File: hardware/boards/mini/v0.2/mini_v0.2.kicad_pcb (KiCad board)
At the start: 8 copper layers, 20 x 41 mm, 100 parts, among them IC1 NAU88C22YG, IC3 IS42S16160J-6BLI, J2 Top, J3 Bottom, Q1 PMV37EN22, U1 W25Q128JVP, U2 LTV-217-G, U4 STM32H750XBHx, Y1 Crystal_GND24, Y3 32.768kHz

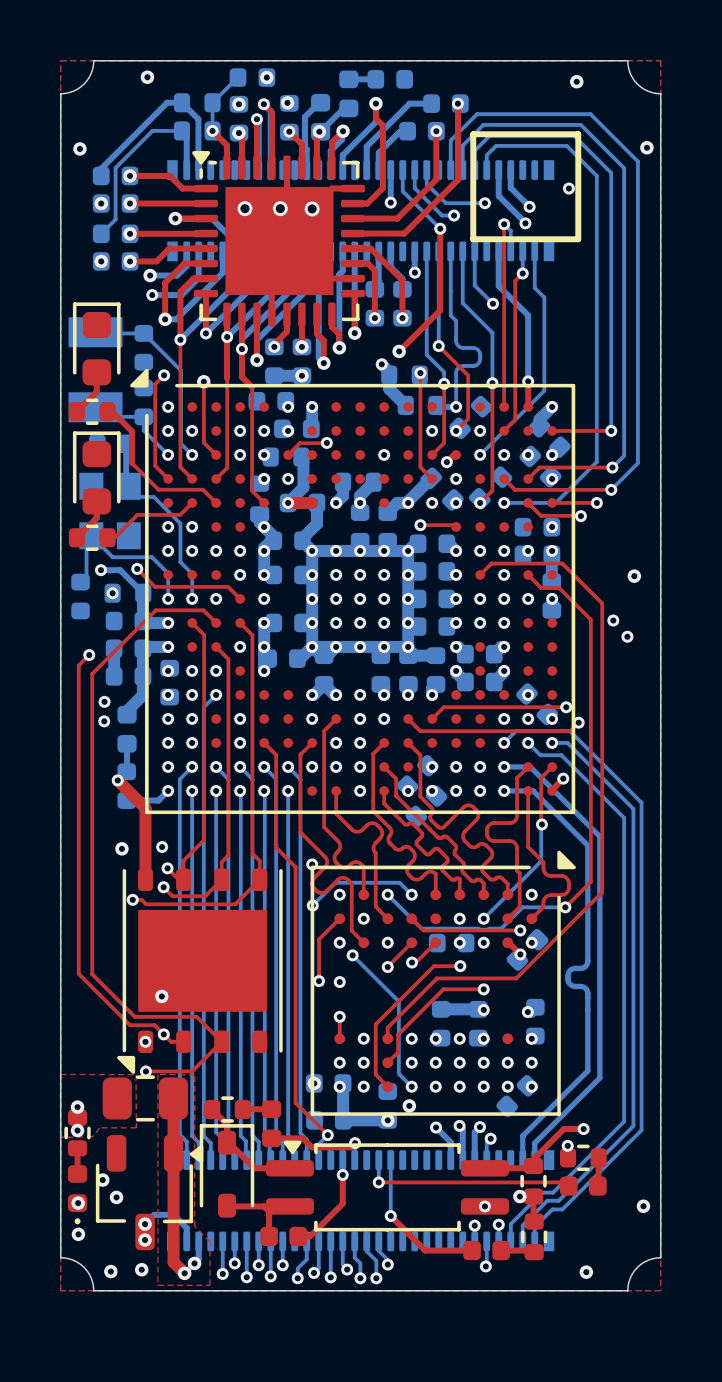
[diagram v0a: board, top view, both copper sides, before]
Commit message: mini: start adding symbol for mating footprint
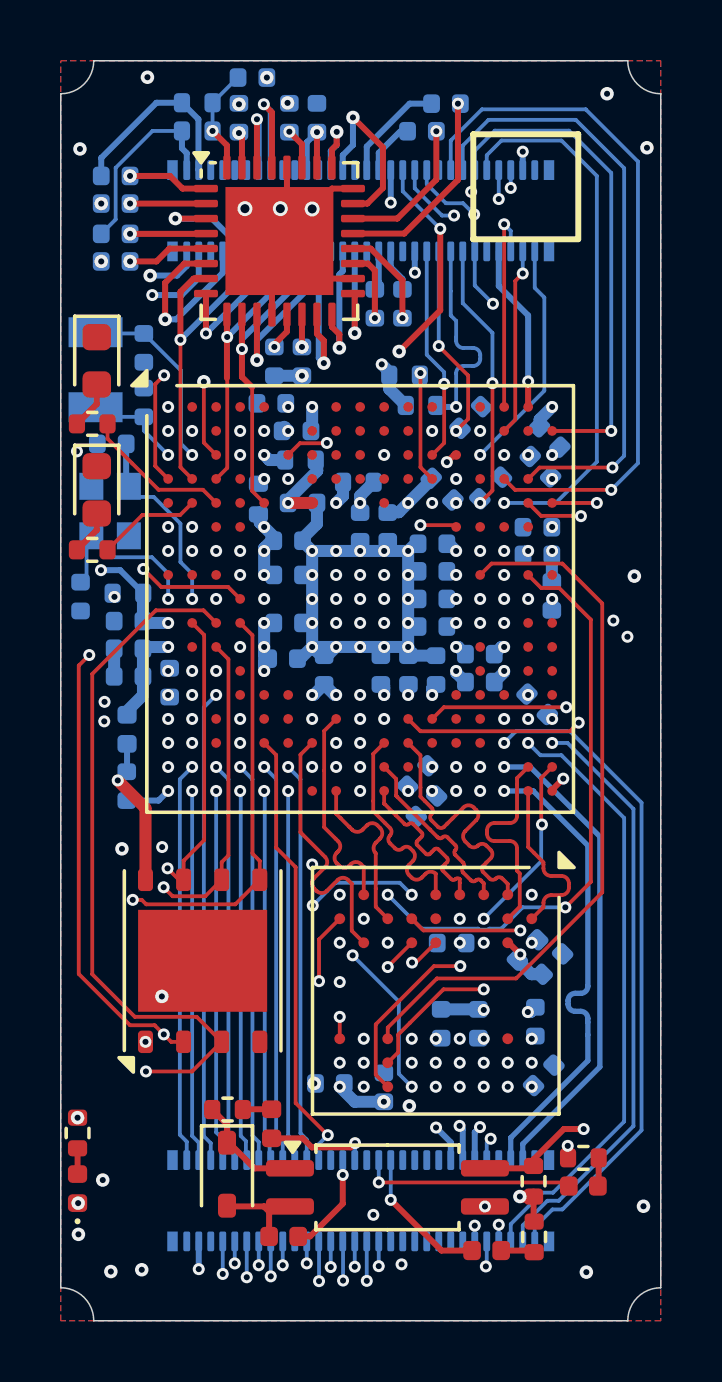
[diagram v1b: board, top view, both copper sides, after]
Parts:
- removed D5, D6: D, Diode_SMD:D_0402_1005Metric
- removed F1: Polyfuse, Fuse:Fuse_0805_2012Metric
- removed Q1: PMV37EN22, Package_TO_SOT_SMD:TSOT-23
- moved C34 9.09 mm to (86.4, 87.1), turned to 45 degrees
- moved C18 2.76 mm to (78.5, 58.9), turned to 90 degrees
- moved C13 1.12 mm to (86.1, 90.8), turned to 45 degrees
- moved C35 0.63 mm to (80.8, 91.2)
- moved R2 0.49 mm to (78.0, 70.3)
- moved D2 0.40 mm to (71.2, 67.0)
- moved R15 0.40 mm to (71.0, 69.1)
- moved D4 0.40 mm to (71.2, 71.3)
- moved R17 0.40 mm to (71.0, 73.3)
- moved C3 0.07 mm to (77.9, 69.3)
- moved C37 0.07 mm to (77.0, 68.4)
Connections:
- C18 pad 1: +3.3V -> /VDDSPK
- IC1 pad 26: Net-(D5-K) -> /VDDSPK
- J2 pad 1: unconnected-(J2-Pad1) -> GND
- J2 pad 10: unconnected-(J2-Pad10) -> GND
- J2 pad 17: unconnected-(J2-Pad17) -> GND
- J2 pad 24: unconnected-(J2-Pad24) -> GND
- J2 pad 3: unconnected-(J2-Pad3) -> +3.3V
- J2 pad 30: unconnected-(J2-Pad30) -> GND
- J2 pad 31: unconnected-(J2-Pad31) -> GND
- J2 pad 36: unconnected-(J2-Pad36) -> GND
- J2 pad 50: unconnected-(J2-Pad50) -> GND
- J2 pad 56: unconnected-(J2-Pad56) -> GND
- J3 pad 1: /USB_D+ -> GND
- J3 pad 14: unconnected-(J3-Pad14) -> GND
- J3 pad 17: unconnected-(J3-Pad17) -> GND
- J3 pad 23: unconnected-(J3-Pad23) -> GND
- J3 pad 26: unconnected-(J3-Pad26) -> GND
- J3 pad 29: unconnected-(J3-Pad29) -> GND
- J3 pad 3: /USB_D- -> /USB_D+
- J3 pad 35: unconnected-(J3-Pad35) -> GND
- J3 pad 42: unconnected-(J3-Pad42) -> GND
- J3 pad 5: unconnected-(J3-Pad5) -> /USB_D-
- J3 pad 56: unconnected-(J3-Pad56) -> GND
- J3 pad 58: /VIN -> +3.3V
- J3 pad 60: /VIN_GND -> GND
- J3 pad 7: unconnected-(J3-Pad7) -> GND
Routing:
- net /VIN: track 7.24 -> 0.00 mm, vias 2 -> 0
- net /VIN_GND: track 2.68 -> 0.00 mm, vias 2 -> 0
- net Net-(D5-K): track 2.49 -> 0.00 mm, vias 1 -> 0
- net /QSPI_IO3: track 28.3 -> 27.3 mm
- net /SPKR: track 6.80 -> 5.88 mm
- net /QSPI_CLK: track 27.4 -> 26.5 mm
- net /QSPI_IO1: track 36.4 -> 35.7 mm
- net /I2C_SDA: track 12.0 -> 12.6 mm
- net /QSPI_IO0: track 29.8 -> 30.4 mm
- net +3.3V: track 48.6 -> 49.2 mm, vias 43 -> 44
- net /QSPI_IO2: track 38.2 -> 38.8 mm
- net /VDDSPK: track 2.47 -> 2.59 mm, vias 0 -> 1
- net GND: vias 85 -> 87
- removed copper zone on F.Cu, net +3.3V
- removed copper zone on F.Cu, net /VIN
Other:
- board size 20 x 41 mm -> 20 x 42 mm
